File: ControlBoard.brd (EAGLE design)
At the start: 100 x 100 mm, 24 parts, among them CON1 USB-BWUERTH-ELECTRONIC-USB-B, IC1 FT232RL

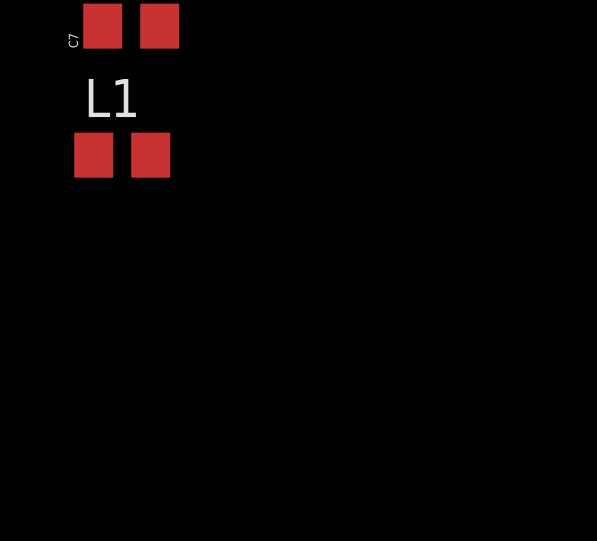
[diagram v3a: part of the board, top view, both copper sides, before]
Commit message: Added leds to RXD/TXD->USB
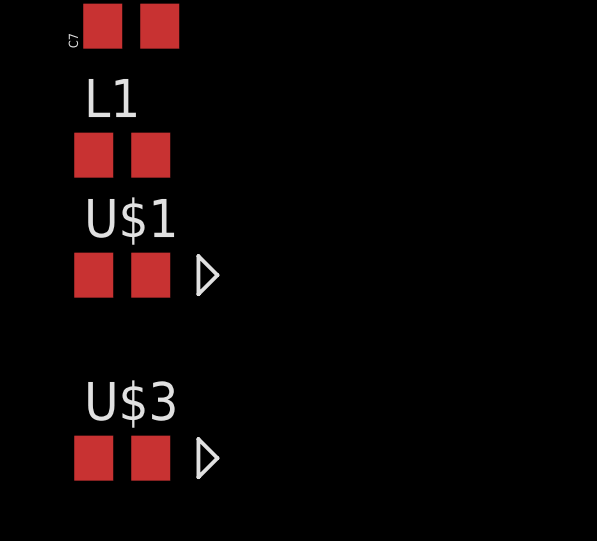
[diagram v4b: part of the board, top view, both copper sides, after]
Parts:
- added U$1, U$3: LED, jogwheelParts:LED_0805
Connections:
- new net N$4: R1.2, U$1.K
- new net N$9: R2.2, U$3.K
- net +5V: now also U$1.A, U$3.A

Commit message: Layout sketch done.
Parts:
- removed U$1, U$3: LED, jogwheelParts:LED_0805
- added RX, TX: LED, jogwheelParts:LED_0805
- moved BTNCON4 149.8 mm to (76.7, 85.0), turned to 90 degrees
- moved L1 148.8 mm to (37.4, 50.9), turned to 270 degrees
- moved C7 139.8 mm to (37.7, 44.3), turned to 270 degrees
- moved R2 130.2 mm to (24.9, 52.3), turned to 270 degrees
- moved R1 128.0 mm to (27.2, 52.3), turned to 270 degrees
- moved BTNCON5 125.0 mm to (76.8, 49.9), turned to 90 degrees
- moved BTNCON1 122.0 mm to (41.5, 85.0), turned to 90 degrees
- moved C5 114.2 mm to (15.3, 35.8)
- moved CON1 113.5 mm to (7.40, 56.0), turned to 90 degrees
- moved C6 106.9 mm to (36.9, 5.50)
- moved BTNCON6 103.5 mm to (76.9, 15.0), turned to 90 degrees
- moved BTNCON2 94.4 mm to (41.9, 50.0), turned to 90 degrees
- moved FERRITE0 85.0 mm to (15.9, 57.8), turned to 270 degrees
- moved IC1 73.4 mm to (25.9, 60.2), turned to 180 degrees
- moved C1 70.6 mm to (19.0, 52.4), turned to 270 degrees
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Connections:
- net +5V: now also RX.A, TX.A; no longer U$1.A, U$3.A
- net N$4: now also RX.K; no longer U$1.K
- net N$9: now also TX.K; no longer U$3.K
